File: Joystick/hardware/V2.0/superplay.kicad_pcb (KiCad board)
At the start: 2 copper layers, 36 parts, among them J1 AVR-PDI-6A, J2 CONN_02X04, J3 USB_B, U1 MCP1700T-3002E, U2 ATXMEGA128A3U-A, U3 TPD4S009DBV, Y1 16MHz

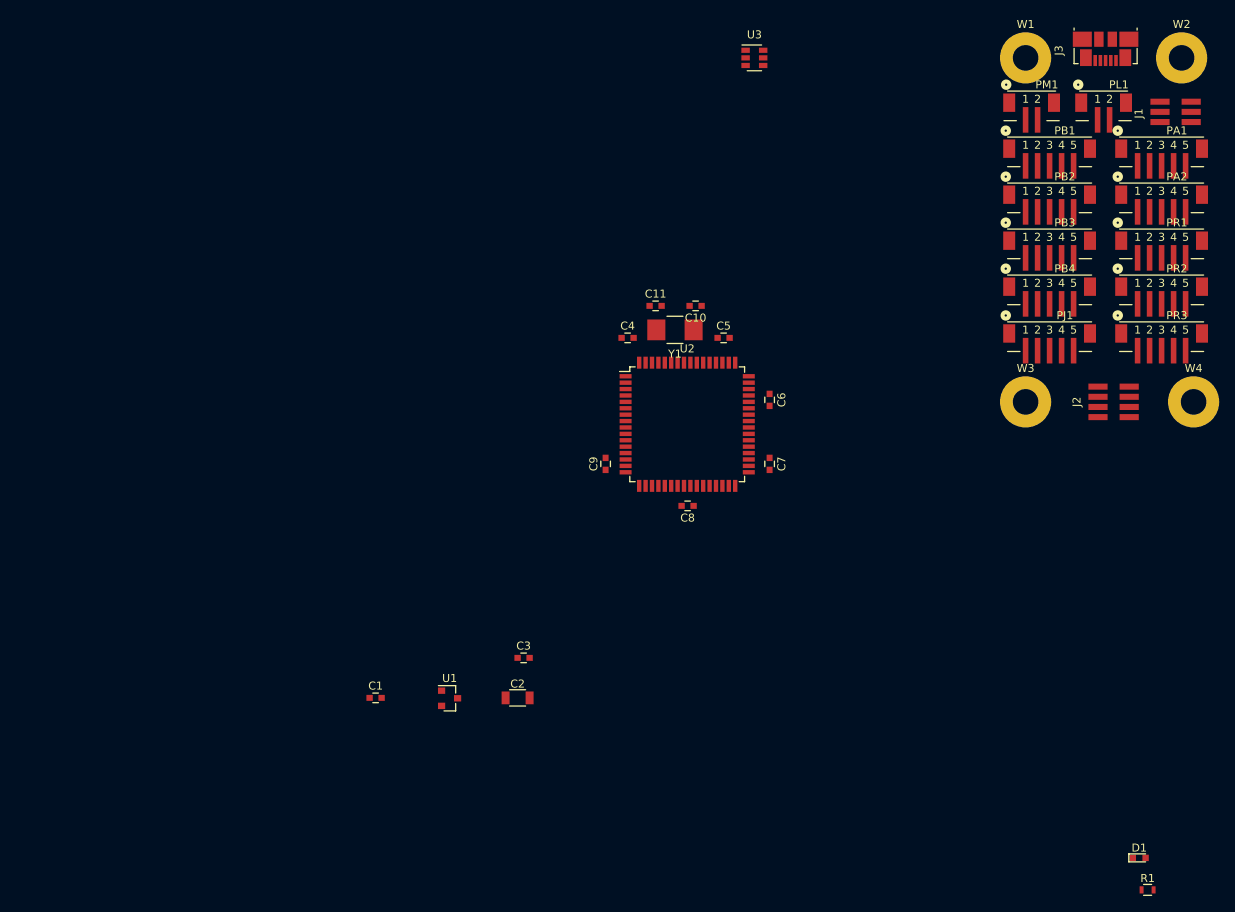
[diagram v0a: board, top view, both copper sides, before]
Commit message: 30x50mm board
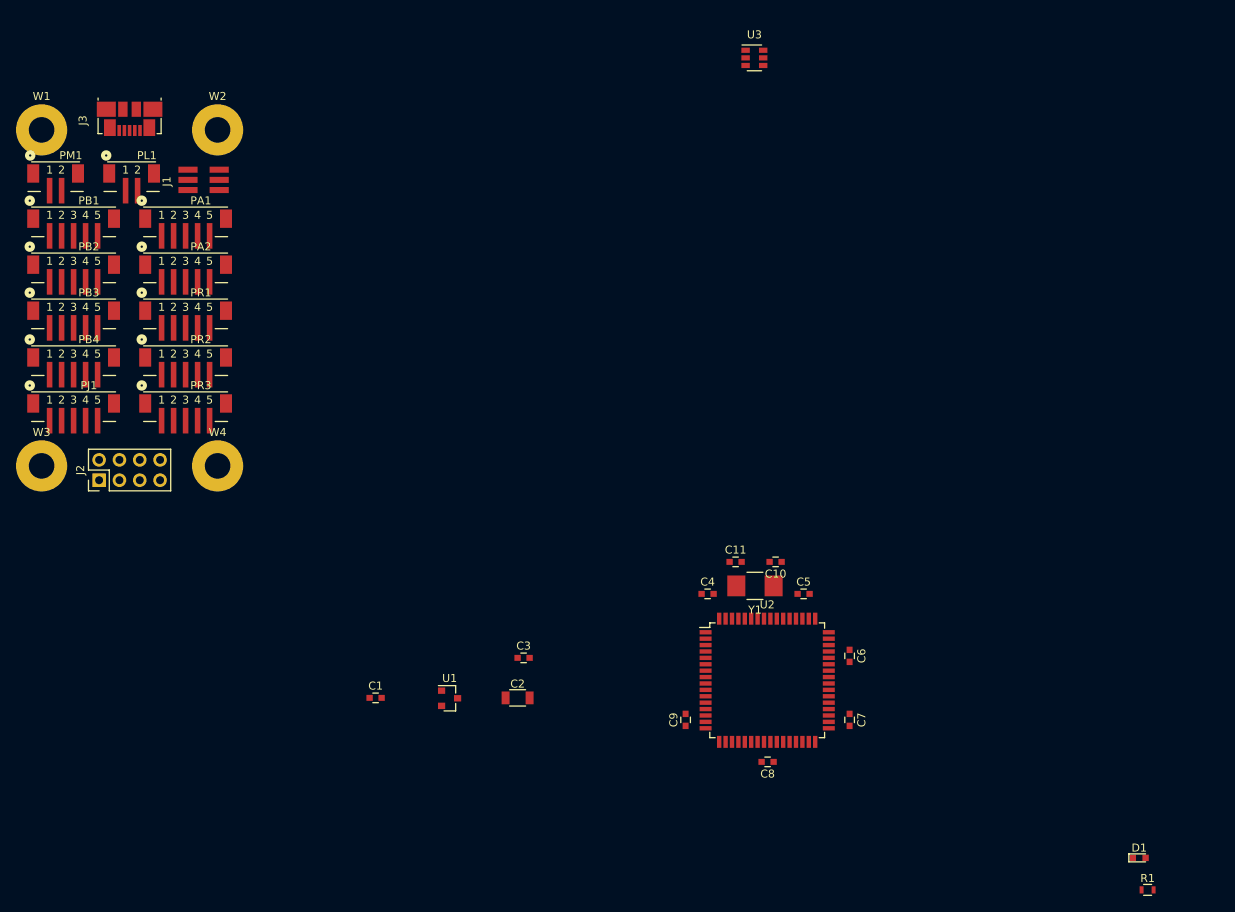
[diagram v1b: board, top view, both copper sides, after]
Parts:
- J2: footprint kuro:4x2_1.27mm_SMD_header -> Pin_Headers:Pin_Header_Straight_2x04_Pitch2.54mm
- moved J2 127.2 mm to (61.2, 97.8)
- moved W1 123.3 mm to (54.0, 54.0)
- moved W3 123.3 mm to (54.0, 96.0)
- moved PB4 122.3 mm to (58.0, 83.0)
- moved PM1 122.3 mm to (55.8, 60.0)
- moved PR2 122.3 mm to (72.0, 83.0)
- moved J3 122.3 mm to (65.0, 52.8)
- moved PA1 122.3 mm to (72.0, 65.7)
- moved PA2 122.3 mm to (72.0, 71.4)
- moved PB1 122.3 mm to (58.0, 65.7)
- moved PB2 122.3 mm to (58.0, 71.4)
- moved PB3 122.3 mm to (58.0, 77.2)
- moved PJ1 122.3 mm to (58.0, 88.8)
- moved PR1 122.3 mm to (72.0, 77.2)
- moved PR3 122.3 mm to (72.0, 88.8)
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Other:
- board text added: "A1"
- board text added: "A2"
- board text added: "B1"
- board text added: "B2"
- board text added: "B3"
- board text added: "B4"
- board text added: "JOY"
- board text added: "LED"
- board text added: "META"
- board text added: "R1"
- board text added: "R2"
- board text added: "R3"

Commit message: Routing attempt
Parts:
- C1, C10, C11, C2, C3, C4, C5, C6, C7, C8, C9, U1, U2, U3, Y1: moved to B.Cu
- moved C8 106.9 mm to (63.0, 64.1)
- moved C7 100.4 mm to (73.2, 69.5), turned to 90 degrees
- moved C9 100.4 mm to (52.8, 69.5), turned to 270 degrees
- moved U2 95.1 mm to (63.0, 74.3)
- moved C6 92.0 mm to (73.2, 77.5), turned to 90 degrees
- moved C4 86.1 mm to (55.5, 85.1)
- moved C5 86.1 mm to (67.5, 85.1)
- moved Y1 85.5 mm to (61.4, 86.1)
- moved C10 83.9 mm to (64.0, 89.1)
- moved C11 83.9 mm to (59.0, 89.1)
- moved U3 78.2 mm to (65.2, 52.0), turned to 90 degrees
- moved C2 63.6 mm to (76.5, 73.2)
- moved U1 62.2 mm to (76.5, 69.8), turned to 90 degrees
- moved C1 61.1 mm to (76.5, 67.0), turned to 180 degrees
- moved C3 58.2 mm to (76.5, 75.8)
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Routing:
- net GND: track 0.00 -> 21.8 mm
- net +3V3: track 0.00 -> 21.3 mm
- net /UP: track 0.00 -> 20.3 mm, vias 0 -> 1
- net /RIGHT: track 0.00 -> 16.0 mm, vias 0 -> 1
- net /B16: track 0.00 -> 15.6 mm, vias 0 -> 1
- net /DOWN: track 0.00 -> 14.1 mm, vias 0 -> 1
- net /LEFT: track 0.00 -> 14.1 mm, vias 0 -> 1
- net /B15: track 0.00 -> 13.3 mm, vias 0 -> 1
- net /B14: track 0.00 -> 11.1 mm, vias 0 -> 1
- net /B13: track 0.00 -> 9.25 mm, vias 0 -> 1
- net Net-(C10-Pad1): track 0.00 -> 9.18 mm
- net /B4: track 0.00 -> 9.15 mm, vias 0 -> 1
- net Net-(C11-Pad1): track 0.00 -> 9.06 mm
- net /B11: track 0.00 -> 7.82 mm, vias 0 -> 1
- net /B10: track 0.00 -> 7.67 mm, vias 0 -> 1
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
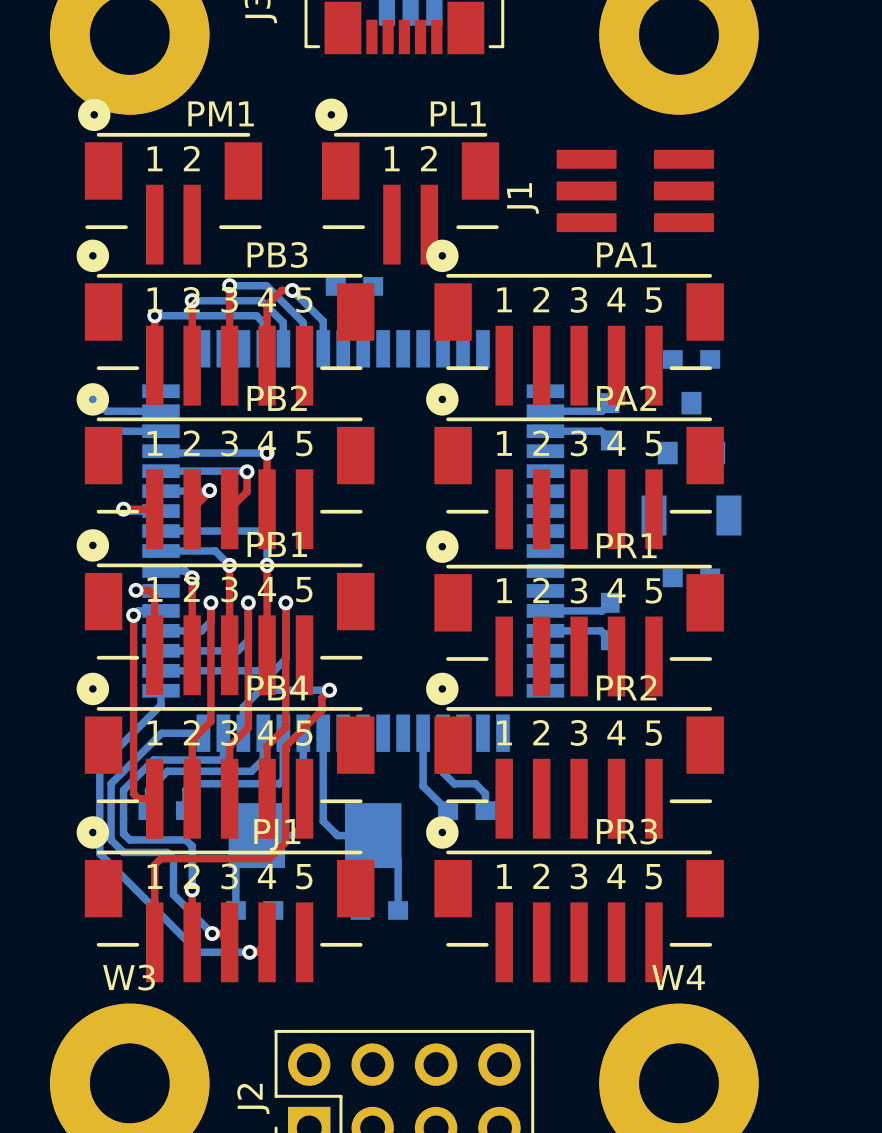
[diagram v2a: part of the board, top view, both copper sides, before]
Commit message: Rewired to make PCB layout easier
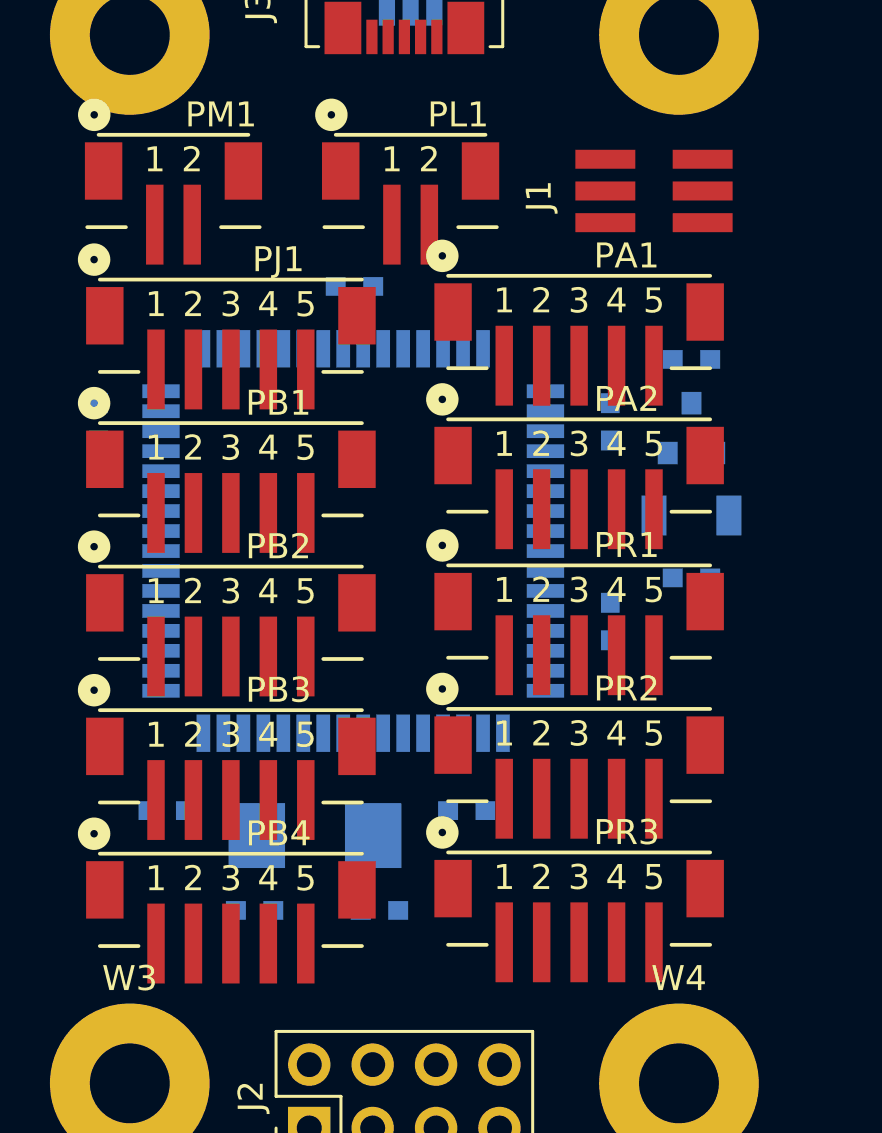
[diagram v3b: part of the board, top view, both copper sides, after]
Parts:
- moved PJ1 23.0 mm to (58.0, 65.8)
- moved PB3 17.4 mm to (58.0, 83.0)
- moved PB2 5.90 mm to (58.0, 77.3)
- moved PB4 5.80 mm to (58.0, 88.8)
- moved PB1 5.70 mm to (58.0, 71.5)
- moved J1 0.75 mm to (75.0, 60.2)
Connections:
- J1 pad 3: (no net) -> Net-(J1-Pad3)
- J1 pad 4: (no net) -> Net-(J1-Pad4)
- U2 pad 1: /RIGHT -> /B13
- U2 pad 10: /B5 -> /B4
- U2 pad 11: /B6 -> /B3
- U2 pad 12: /B7 -> /B2
- U2 pad 13: /B8 -> /B1
- U2 pad 2: /B16 -> /B12
- U2 pad 20: /B9 -> /UP
- U2 pad 21: /B10 -> /DOWN
- U2 pad 22: /B11 -> /LEFT
- U2 pad 23: /B12 -> /RIGHT
- U2 pad 26: /A5 -> /A1
- U2 pad 27: /A6 -> /A2
- U2 pad 28: /A7 -> /A3
- U2 pad 29: /A8 -> /A4
- U2 pad 3: /B15 -> /B11
- U2 pad 36: /R1 -> /A8
- U2 pad 37: /R2 -> /A7
- U2 pad 38: /R3 -> /A6
- U2 pad 39: /R4 -> /A5
- U2 pad 4: /B14 -> /B10
- U2 pad 40: /R5 -> /R4
- U2 pad 41: /R6 -> /R3
- U2 pad 42: /R7 -> /R2
- U2 pad 43: /R8 -> /R1
- U2 pad 46: /R9 -> /R8
- U2 pad 47: /R10 -> /R7
- U2 pad 48: /R11 -> /R6
- U2 pad 49: /R12 -> /R5
- U2 pad 5: /B13 -> /B9
- U2 pad 50: /A1 -> /R12
- U2 pad 51: /A2 -> /R11
- U2 pad 54: /A3 -> /R10
- U2 pad 55: /A4 -> /R9
- U2 pad 6: /B1 -> /B8
- U2 pad 62: /UP -> /B16
- U2 pad 63: /DOWN -> /B15
- U2 pad 64: /LEFT -> /B14
- U2 pad 7: /B2 -> /B7
- U2 pad 8: /B3 -> /B6
- U2 pad 9: /B4 -> /B5
- U3 pad 4: (no net) -> Net-(U3-Pad4)
- U3 pad 6: (no net) -> Net-(U3-Pad6)
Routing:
- net GND: track 21.8 -> 0.00 mm
- net +3V3: track 21.3 -> 0.00 mm
- net /UP: track 20.3 -> 0.00 mm, vias 1 -> 0
- net /RIGHT: track 16.0 -> 0.00 mm, vias 1 -> 0
- net /B16: track 15.6 -> 0.00 mm, vias 1 -> 0
- net /DOWN: track 14.1 -> 0.00 mm, vias 1 -> 0
- net /LEFT: track 14.1 -> 0.00 mm, vias 1 -> 0
- net /B15: track 13.3 -> 0.00 mm, vias 1 -> 0
- net /B14: track 11.1 -> 0.00 mm, vias 1 -> 0
- net /B13: track 9.25 -> 0.00 mm, vias 1 -> 0
- net Net-(C10-Pad1): track 9.18 -> 0.00 mm
- net /B4: track 9.15 -> 0.00 mm, vias 1 -> 0
- net Net-(C11-Pad1): track 9.06 -> 0.00 mm
- net /B11: track 7.82 -> 0.00 mm, vias 1 -> 0
- net /B10: track 7.67 -> 0.00 mm, vias 1 -> 0
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
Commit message: Routing looks successful
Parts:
- moved R1 161.0 mm to (60.2, 56.8), turned to 180 degrees
- moved D1 155.0 mm to (63.8, 56.8)
- moved C1 7.25 mm to (76.5, 59.8), turned to 0 degrees
- moved C2 7.25 mm to (76.5, 66.0)
- moved C3 7.25 mm to (76.5, 68.5)
- moved U1 7.25 mm to (76.5, 62.5)
- moved PA1 0.15 mm to (72.0, 65.8)
- moved PA2 0.15 mm to (72.0, 71.5)
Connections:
- U2 pad 26: /A1 -> /META
- U2 pad 27: /A2 -> /LED
- U2 pad 28: /A3 -> /A4
- U2 pad 29: /A4 -> /A3
- U2 pad 30: /META -> /A2
- U2 pad 31: /LED -> /A1
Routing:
- net Net-(J1-Pad5): track 0.00 -> 37.4 mm, vias 0 -> 1
- net Net-(J2-Pad8): track 0.00 -> 36.4 mm, vias 0 -> 1
- net Net-(J2-Pad4): track 0.00 -> 35.8 mm, vias 0 -> 1
- net Net-(J2-Pad6): track 0.00 -> 35.6 mm, vias 0 -> 1
- net Net-(J2-Pad2): track 0.00 -> 34.9 mm, vias 0 -> 1
- net Net-(J1-Pad1): track 0.00 -> 32.3 mm, vias 0 -> 1
- net GND: track 0.00 -> 24.4 mm, vias 0 -> 2
- net +3V3: track 0.00 -> 21.2 mm
- net /B16: track 0.00 -> 20.9 mm, vias 0 -> 1
- net /B10: track 0.00 -> 17.7 mm, vias 0 -> 1
- net /B11: track 0.00 -> 15.9 mm, vias 0 -> 1
- net /B15: track 0.00 -> 15.5 mm, vias 0 -> 1
- net /B12: track 0.00 -> 15.4 mm, vias 0 -> 1
- net /A4: track 0.00 -> 12.9 mm, vias 0 -> 1
- net /R10: track 0.00 -> 12.0 mm, vias 0 -> 1
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- added copper zone on GND, net GND
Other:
- copper layers 2 -> 4

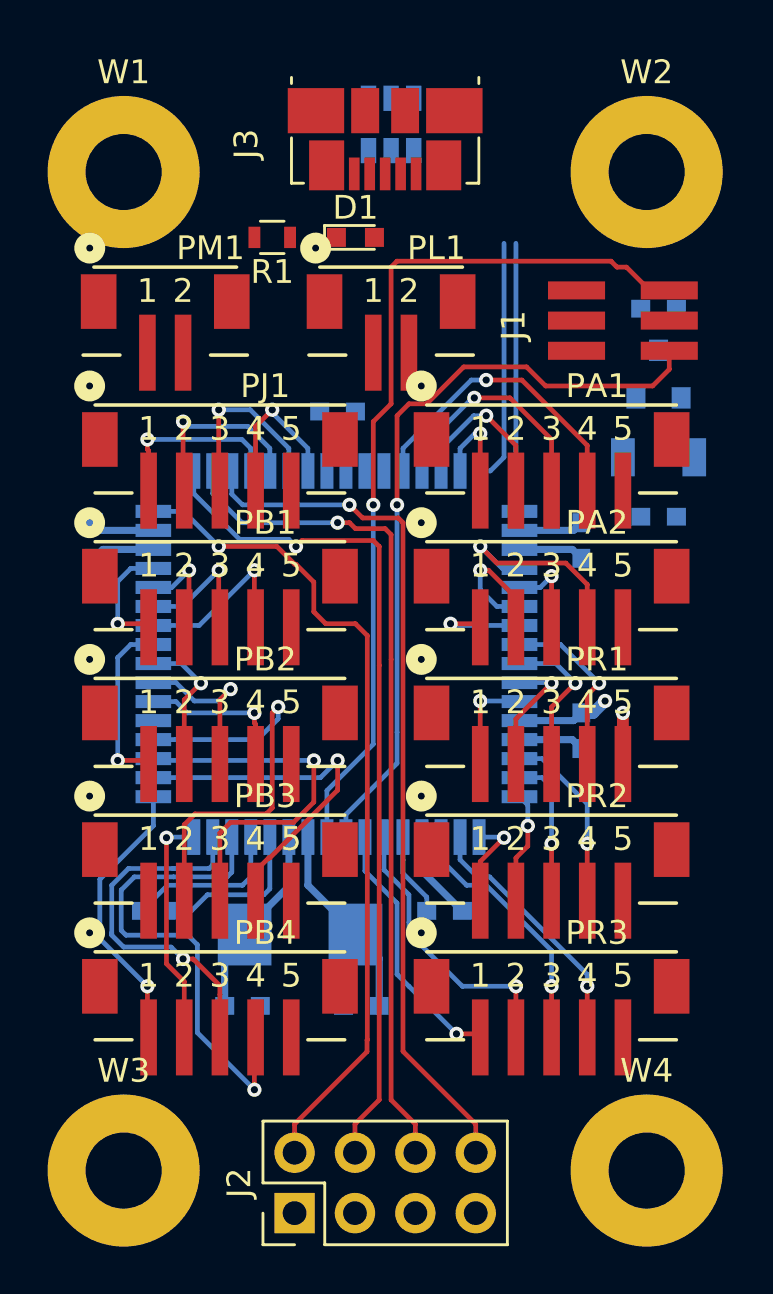
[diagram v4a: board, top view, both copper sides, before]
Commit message: Routing power
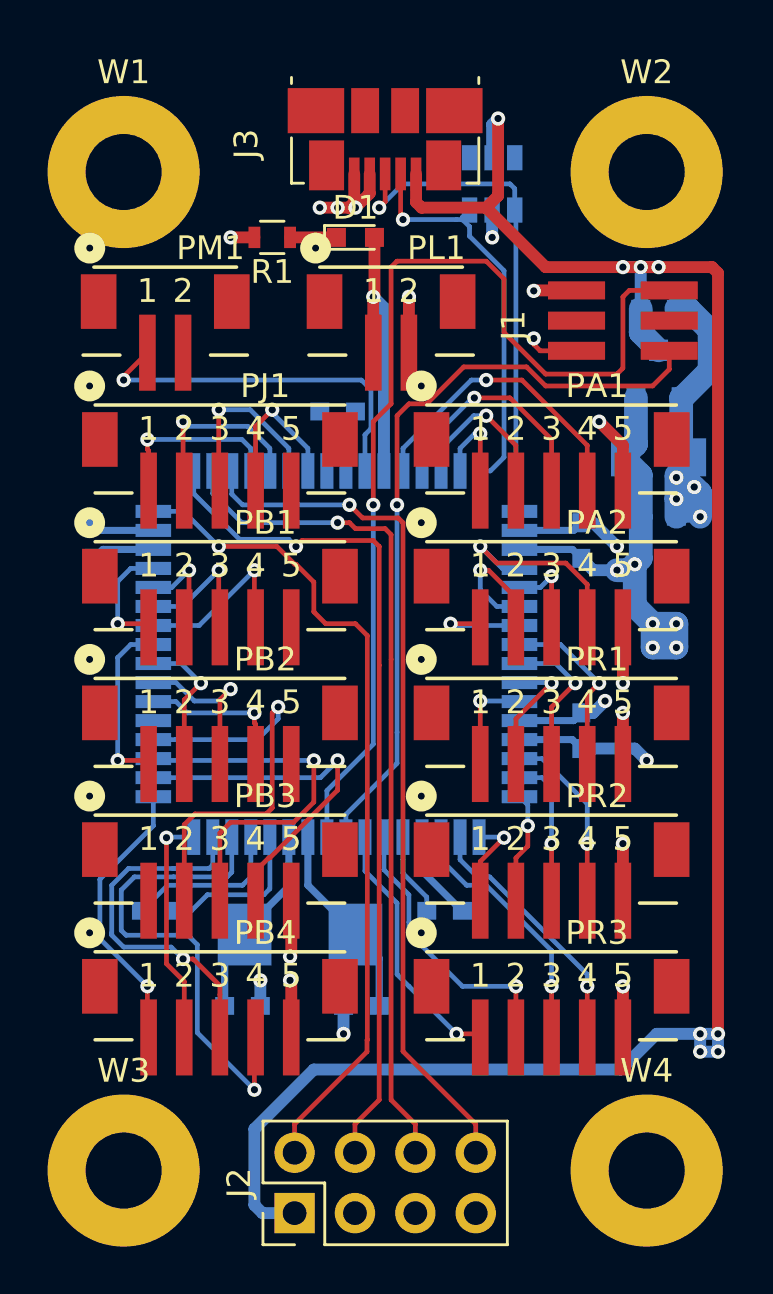
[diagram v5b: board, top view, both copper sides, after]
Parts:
- moved U3 4.93 mm to (69.5, 54.5)
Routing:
- net +5V: track 0.00 -> 86.6 mm, vias 0 -> 8
- net GND: track 24.4 -> 68.6 mm, vias 2 -> 22
- net +3V3: track 21.2 -> 43.3 mm, vias 0 -> 8
- net /META: track 0.00 -> 15.7 mm, vias 0 -> 1
- net /LED: track 0.00 -> 12.4 mm, vias 0 -> 1
- net Net-(J3-Pad3): track 11.3 -> 21.4 mm, vias 0 -> 1
- net Net-(J3-Pad2): track 10.3 -> 17.0 mm, vias 0 -> 1
- net Net-(J1-Pad5): track 37.4 -> 43.4 mm
- net Net-(D1-Pad1): track 0.00 -> 1.95 mm
- added copper zone on PWR, net +3V3
